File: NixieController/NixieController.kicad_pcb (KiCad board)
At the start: 2 copper layers, 156.5 x 67.5 mm, 87 parts, among them J1 Conn_02x05_Odd_Even, J10 Conn_01x06, J11 Conn_01x05, J12 Barrel_Jack, J13 Conn_02x05_Odd_Even, J14 Conn_02x05_Odd_Even, J15 Conn_02x05_Odd_Even, J16 Conn_01x07, J17 Conn_01x04, J18 Conn_01x02, J2 Conn_01x01, J3 Conn_01x01, J4 Conn_01x01, J5 Conn_01x01, J6 Conn_01x04, J8 Conn_01x04, Q1 2N2222A, Q2 2N2222A, Q3 2N2222A, Q4 2N2222A, SW1 SW_Push, SW2 SW_Push, SW3 SW_Push, U2 L7805

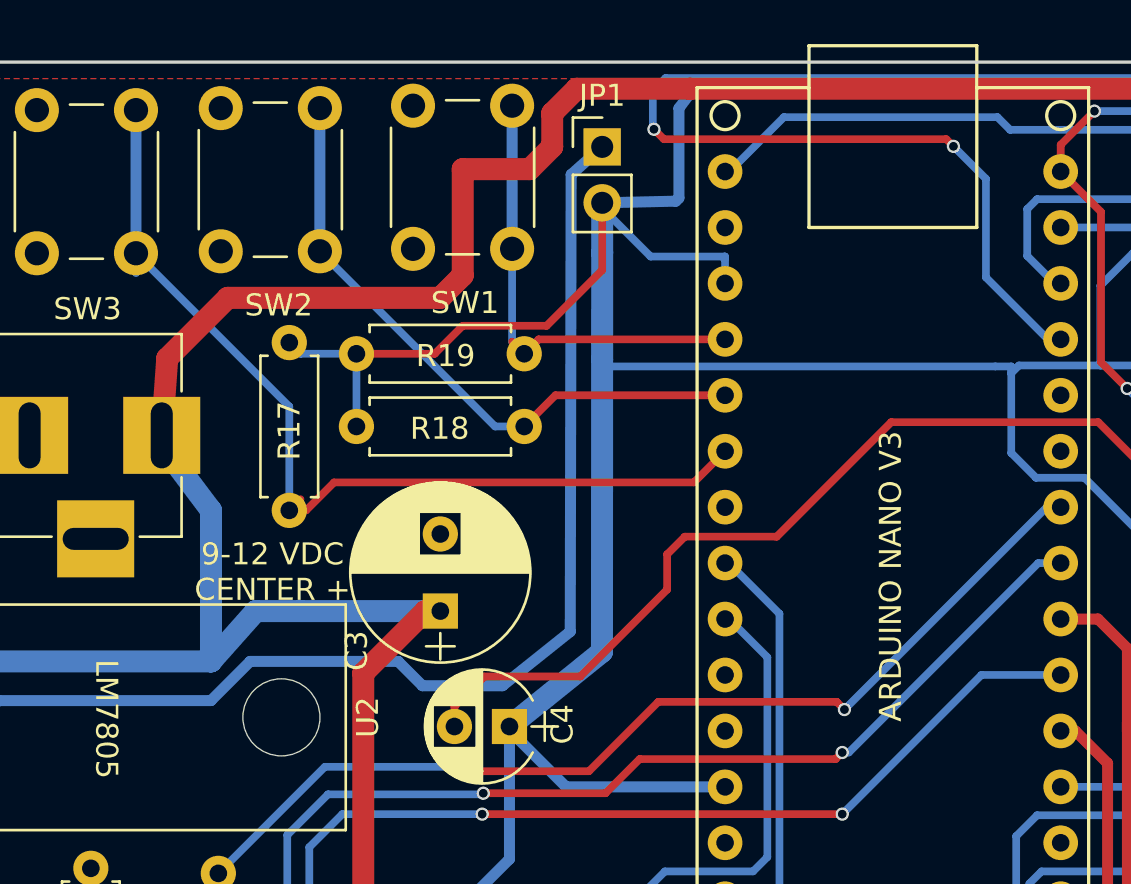
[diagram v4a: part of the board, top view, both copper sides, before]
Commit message: Added capacitors to buttons to filter noise
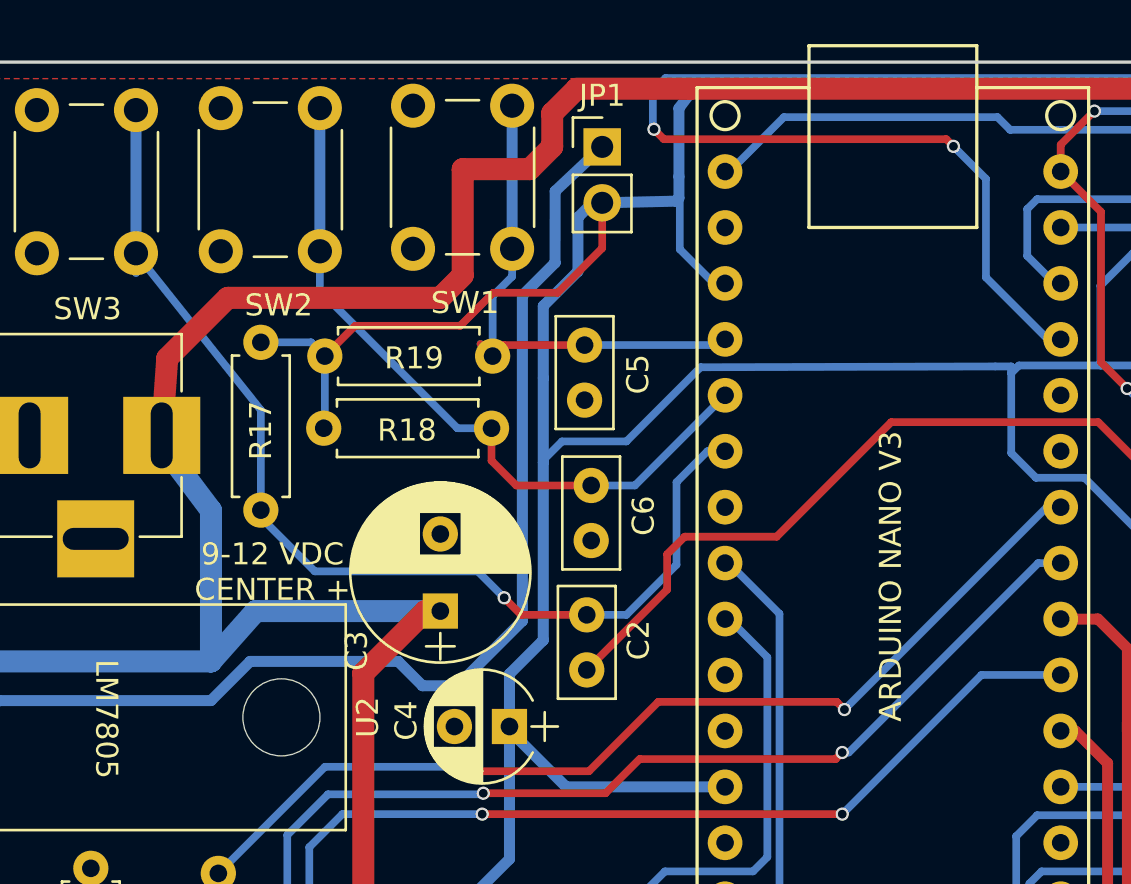
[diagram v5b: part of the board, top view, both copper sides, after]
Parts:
- added C2: 10 nF, Capacitors_THT:C_Disc_D5.0mm_W2.5mm_P2.50mm, F.Cu at (146.0, 76.5)
- added C5: 10 nF, Capacitors_THT:C_Disc_D5.0mm_W2.5mm_P2.50mm, F.Cu at (145.9, 64.2)
- added C6: 10 nF, Capacitors_THT:C_Disc_D5.0mm_W2.5mm_P2.50mm, F.Cu at (146.2, 70.6)
- moved R18 1.49 mm to (141.7, 65.5)
- moved R19 1.44 mm to (141.7, 62.2)
- moved R17 1.29 mm to (131.2, 61.6)
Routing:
- net GND: track 109.1 -> 101.9 mm
- net BUTTON3: track 43.6 -> 50.5 mm, vias 0 -> 1
- net BUTTON2: track 30.0 -> 34.3 mm
- net +5V: track 435.7 -> 439.0 mm
- net BUTTON1: track 22.2 -> 24.7 mm
- net Net-(JP1-Pad1): track 56.4 -> 55.0 mm
